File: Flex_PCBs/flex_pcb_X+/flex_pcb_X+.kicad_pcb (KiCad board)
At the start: 2 copper layers, 4.5 x 51 mm, 2 parts, among them J1 Conn_01x08_Male, J2 Conn_01x08_Male

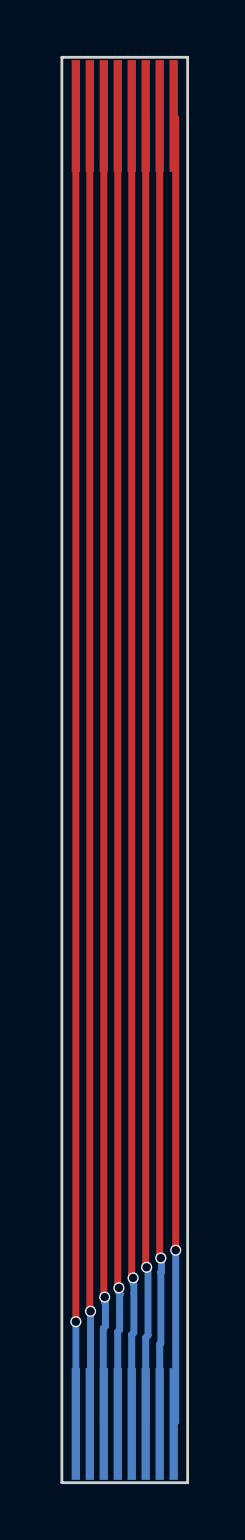
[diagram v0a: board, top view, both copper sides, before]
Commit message: Added small modifications to the existing flex PCBs plus the new ones: Y- and X-.
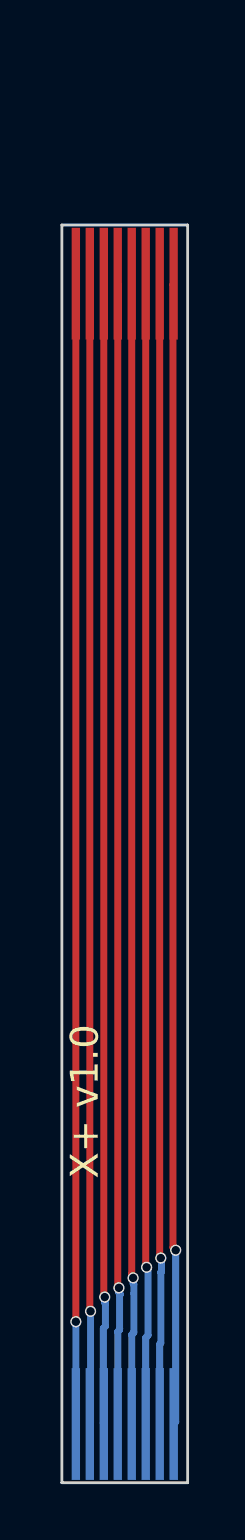
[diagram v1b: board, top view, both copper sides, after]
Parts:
- moved J1 6.00 mm to (126.0, 90.1)
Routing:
- net 8: track 46.8 -> 40.8 mm
- net 7: track 46.8 -> 40.8 mm
- net 6: track 46.9 -> 40.9 mm
- net 5: track 46.9 -> 40.9 mm
- net 3: track 46.9 -> 40.9 mm
- net 2: track 46.9 -> 40.9 mm
- net 1: track 46.9 -> 40.9 mm
- net 4: track 46.8 -> 41.0 mm
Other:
- board size 4.5 x 51 mm -> 4.5 x 45 mm
- board text added: "X+ v1.0"
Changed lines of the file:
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@@
-(kicad_pcb (version 20211014) (generator pcbnew)
+(kicad_pcb (version 20221018) (generator pcbnew)
   (general
     (thickness 1.6)
@@
     (pcbplotparams
       (layerselection 0x00410fc_ffffffff)
+      (plot_on_all_layers_selection 0x0000000_00000000)
       (disableapertmacros false)
       (usegerberextensions true)
@@
       (usegerberadvancedattributes false)
       (creategerberjobfile false)
-      (svguseinch false)
+      (dashed_line_dash_ratio 12.000000)
+      (dashed_line_gap_ratio 3.000000)
       (svgprecision 6)
-      (excludeedgelayer true)
       (plotframeref false)
       (viasonmask false)
@@
       (drillshape 0)
       (scaleselection 1)
-      (outputdirectory "")
+      (outputdirectory "/home/stefan/DEV/spaceteam/gerber/X+/")
     )
   )
@@
   (net 8 "1")
   (footprint "STS_connector:flexpcb con." (layer "F.Cu")
-    (at 126 84.1)
+    (at 126 90.1)
     (property "Sheetfile" "flex_pcb_X+.kicad_sch")
     (property "Sheetname" "")
     (attr smd)
     (fp_text reference "J1" (at -16.51 -3.81 unlocked) (layer "F.SilkS") hide
-      (effects (font (size 1 1) (thickness 0.15)))
+        (effects (font (size 1 1) (thickness 0.15)))
     )
     (fp_text value "Conn_01x08_Male" (at -16.51 -2.31 unlocked) (layer "F.Fab")
-      (effects (font (size 1 1) (thickness 0.15)))
+        (effects (font (size 1 1) (thickness 0.15)))
     )
     (fp_text user "${REFERENCE}" (at -16.51 -0.81 unlocked) (layer "F.Fab")
-      (effects (font (size 1 1) (thickness 0.15)))
+        (effects (font (size 1 1) (thickness 0.15)))
     )
     (pad "1" smd rect (at 0.5 -2) (size 0.3 4) (layers "F.Cu" "F.Paste" "F.Mask")
@@
     (attr smd)
     (fp_text reference "J2" (at -16.51 3.81 unlocked) (layer "B.SilkS") hide
-      (effects (font (size 1 1) (thickness 0.15)) (justify mirror))
+        (effects (font (size 1 1) (thickness 0.15)) (justify mirror))
     )
     (fp_text value "Conn_01x08_Male" (at -16.51 2.31 unlocked) (layer "B.Fab")
-      (effects (font (size 1 1) (thickness 0.15)) (justify mirror))
+        (effects (font (size 1 1) (thickness 0.15)) (justify mirror))
     )
     (fp_text user "${REFERENCE}" (at -16.51 0.81 unlocked) (layer "B.Fab")
-      (effects (font (size 1 1) (thickness 0.15)) (justify mirror))
+        (effects (font (size 1 1) (thickness 0.15)) (justify mirror))
     )
     (pad "1" smd rect (at 0.5 2 180) (size 0.3 4) (layers "B.Cu" "B.Paste" "B.Mask")
@@
       (net 1 "8") (pinfunction "Pin_8") (pintype "passive"))
   )
-  (gr_line (start 130.5 80) (end 130.5 131) (layer "Edge.Cuts") (width 0.1))
-  (gr_line (start 126 80) (end 126 131) (layer "Edge.Cuts") (width 0.1))
-  (gr_line (start 126 131) (end 130.5 131) (layer "Edge.Cuts") (width 0.1))
-  (gr_line (start 126 80) (end 130.5 80) (layer "Edge.Cuts") (width 0.1))
-  (gr_rect (start 126 131) (end 130.5 121.74) (layer "User.1") (width 0.15) (fill none))
-  (gr_rect (start 126 89.2628) (end 130.5 80) (layer "User.1") (width 0.15) (fill none))
-  (gr_text "The PCB should have \na thickness of 0.12 mm (two Layer).\nOn the marked areas in User.1 layer a 0.225 mm polyimide stiffener\nshould be glued.\nThe resulting gold fingers should have 0.3 mm in thickness.\n\n\n" (at 157.4546 89.0016) (layer "User.1")
+  (gr_line (start 130.5 86) (end 130.5 131)
+    (stroke (width 0.1) (type solid)) (layer "Edge.Cuts"))
+  (gr_line (start 126 86) (end 126 131)
+    (stroke (width 0.1) (type solid)) (layer "Edge.Cuts"))
+  (gr_line (start 126 131) (end 130.5 131)
+    (stroke (width 0.1) (type solid)) (layer "Edge.Cuts"))
+  (gr_line (start 126 86) (end 130.5 86)
+    (stroke (width 0.1) (type solid)) (layer "Edge.Cuts"))
+  (gr_rect (start 126 121.74) (end 130.5 131)
+    (stroke (width 0.15) (type solid)) (fill none) (layer "User.1"))
+  (gr_rect (start 126 86) (end 130.5 95.2628)
+    (stroke (width 0.15) (type solid)) (fill none) (layer "User.1"))
+  (gr_text "X+ v1.0\n" (at 127.4064 120.1166 90) (layer "F.SilkS")
+    (effects (font (size 1 1) (thickness 0.15)) (justify left bottom))
+  )
+  (gr_text "The PCB should have \na thickness of 0.12 mm (two Layer).\nOn the marked areas in User.1 layer a 0.225 mm polyimide stiffener\nshould be glued.\nThe resulting gold fingers should have 0.3 mm in thickness.\n\n\n" (at 158.6738 91.8464) (layer "User.1")
     (effects (font (size 1 1) (thickness 0.15)))
   )
@@
     (effects (font (size 1 1) (thickness 0.15)))
   )
-  (segment (start 126.5 82.1) (end 126.5 125.2394) (width 0.25) (layer "F.Cu") (net 1))
+  (segment (start 126.5 88.1) (end 126.5 125.2394) (width 0.25) (layer "F.Cu") (net 1))
   (via (at 126.5 125.2394) (size 0.4) (drill 0.3) (layers "F.Cu" "B.Cu") (net 1))
   (segment (start 126.5 125.2394) (end 126.5 128.9) (width 0.25) (layer "B.Cu") (net 1))
+  (segment (start 127 124.841) (end 127 88.1) (width 0.25) (layer "F.Cu") (net 2))
   (segment (start 127 124.841) (end 127.0254 124.8664) (width 0.25) (layer "F.Cu") (net 2))
-  (segment (start 127 82.1) (end 127 124.841) (width 0.25) (layer "F.Cu") (net 2))
   (via (at 127.0254 124.8664) (size 0.4) (drill 0.3) (layers "F.Cu" "B.Cu") (net 2))
   (segment (start 127.0254 124.8664) (end 127.0254 128.8746) (width 0.25) (layer "B.Cu") (net 2))
   (segment (start 127.0254 128.8746) (end 127 128.9) (width 0.25) (layer "B.Cu") (net 2))
-  (segment (start 127.5 82.1) (end 127.5 124.325) (width 0.25) (layer "F.Cu") (net 3))
   (segment (start 127.5 124.325) (end 127.5334 124.3584) (width 0.25) (layer "F.Cu") (net 3))
+  (segment (start 127.5 124.325) (end 127.5 88.1) (width 0.25) (layer "F.Cu") (net 3))
   (via (at 127.5334 124.3584) (size 0.4) (drill 0.3) (layers "F.Cu" "B.Cu") (net 3))
   (segment (start 127.4826 125.476) (end 127.4826 128.8826) (width 0.25) (layer "B.Cu") (net 3))
@@
   (segment (start 127.5588 125.3998) (end 127.4826 125.476) (width 0.25) (layer "B.Cu") (net 3))
   (segment (start 128 123.9868) (end 128.0414 124.0282) (width 0.25) (layer "F.Cu") (net 4))
-  (segment (start 128 82.1) (end 128 123.9868) (width 0.25) (layer "F.Cu") (net 4))
+  (segment (start 128 123.9868) (end 128 88.1) (width 0.25) (layer "F.Cu") (net 4))
   (via (at 128.0414 124.0282) (size 0.4) (drill 0.3) (layers "F.Cu" "B.Cu") (net 4))
   (segment (start 128.0668 124.2822) (end 128.0922 124.2568) (width 0.25) (layer "B.Cu") (net 4))
@@
   (segment (start 128 128.9) (end 128 125.5936) (width 0.25) (layer "B.Cu") (net 4))
   (segment (start 128.5 123.5442) (end 128.4986 123.5456) (width 0.25) (layer "F.Cu") (net 5))
+  (segment (start 128.5494 123.6726) (end 128.5 123.6232) (width 0.25) (layer "F.Cu") (net 5))
   (segment (start 128.4986 123.6218) (end 128.5494 123.6726) (width 0.25) (layer "F.Cu") (net 5))
   (segment (start 128.4986 123.5456) (end 128.4986 123.6218) (width 0.25) (layer "F.Cu") (net 5))
-  (segment (start 128.5 82.1) (end 128.5 123.5442) (width 0.25) (layer "F.Cu") (net 5))
+  (segment (start 128.5 123.6232) (end 128.5 88.1) (width 0.25) (layer "F.Cu") (net 5))
   (via (at 128.5494 123.6726) (size 0.4) (drill 0.3) (layers "F.Cu" "B.Cu") (net 5))
   (segment (start 128.5748 123.9012) (end 128.5748 124.206) (width 0.25) (layer "B.Cu") (net 5))
@@
   (segment (start 128.5494 123.8758) (end 128.5748 123.9012) (width 0.25) (layer "B.Cu") (net 5))
   (segment (start 129 123.2596) (end 129.032 123.2916) (width 0.25) (layer "F.Cu") (net 6))
-  (segment (start 129 82.1) (end 129 123.2596) (width 0.25) (layer "F.Cu") (net 6))
+  (segment (start 129 123.2596) (end 129 88.1) (width 0.25) (layer "F.Cu") (net 6))
   (via (at 129.032 123.2916) (size 0.4) (drill 0.3) (layers "F.Cu" "B.Cu") (net 6))
   (segment (start 129.0828 123.3424) (end 129.032 123.2916) (width 0.25) (layer "B.Cu") (net 6))
@@
   (segment (start 129 125.8128) (end 129.0828 125.73) (width 0.25) (layer "B.Cu") (net 6))
   (segment (start 129.0828 125.73) (end 129.0828 123.3424) (width 0.25) (layer "B.Cu") (net 6))
-  (segment (start 129.5 82.1) (end 129.5 122.9214) (width 0.25) (layer "F.Cu") (net 7))
+  (segment (start 129.5 88.1) (end 129.5 122.9214) (width 0.25) (layer "F.Cu") (net 7))
   (segment (start 129.5 122.9214) (end 129.54 122.9614) (width 0.25) (layer "F.Cu") (net 7))
   (via (at 129.54 122.9614) (size 0.4) (drill 0.3) (layers "F.Cu" "B.Cu") (net 7))
@@
   (segment (start 129.54 123.4694) (end 129.5654 123.444) (width 0.25) (layer "B.Cu") (net 7))
   (segment (start 129.5654 123.444) (end 129.5654 122.9868) (width 0.25) (layer "B.Cu") (net 7))
-  (segment (start 130.0734 122.682) (end 130.0734 82.1734) (width 0.25) (layer "F.Cu") (net 8))
-  (segment (start 130.0734 82.1734) (end 130 82.1) (width 0.25) (layer "F.Cu") (net 8))
+  (segment (start 130 88.1) (end 129.975 88.125) (width 0.25) (layer "F.Cu") (net 8))
+  (segment (start 129.975 88.125) (end 129.975 122.5836) (width 0.25) (layer "F.Cu") (net 8))
+  (segment (start 129.975 122.5836) (end 130.0734 122.682) (width 0.25) (layer "F.Cu") (net 8))
   (via (at 130.0734 122.682) (size 0.4) (drill 0.3) (layers "F.Cu" "B.Cu") (net 8))
   (segment (start 130.0734 122.682) (end 130.0734 128.8266) (width 0.25) (layer "B.Cu") (net 8))
